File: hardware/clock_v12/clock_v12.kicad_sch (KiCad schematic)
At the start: 225 parts, among them J1 RJ45, J12 Conn_01x08_Pin, J14 Conn_01x02_Pin, J2 Conn_01x03, J4 USB_C_Receptacle, J5 Conn_01x06_Pin, J6 Conn_01x03_Pin, J8 Conn_01x02_Pin, Q1 2N7002, Q10 2N7002, Q9 2N7002, SW1 SW_Push_4PDT, SW2 SW_SPDT, U1 ADA4807-1, U10 STM32F405RGTx, U11 AMS1117-3.3, U12 BA50DD0WHFP-TR, U13 M24C02-RMN, U14 CH340C, U15 USBLC6-2P6, U16 TLV3603DCKR, U17 SN74LVC1G14DBV, U18 TMP112AIDRLR, U19 SN74LVC1G14DBV, U2 SN74LVC1G14DBV, U20 SN74LVC1G14DBV, U21 SN74LVC1G14DBV, U23 TPS63060, U3 SN74LVC1G14DBV, U4 ADA4807-1, U5 ADA4807-1, U6 TLV3603DCKR, U7 SN74LVC1G14DBV, U8 TLV3603DCKR, U9 L78L05_SOT89, Y1 MultiOsc, Y2 16MHz

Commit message: add 3d model for RJ45 connector
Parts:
- J1: footprint Connector_RJ:RJ45_Amphenol_RJHSE5380 -> blinky_footprints:RJ45_Amphenol_RJHSE5380
- J4: footprint Connector_USB:USB_C_Receptacle_HRO_TYPE-C-31-M-12 -> blinky_footprints:USB_C_Receptacle_HRO_TYPE-C-31-M-12
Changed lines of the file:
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@@
 			)
 		)
-		(property "Footprint" "Connector_USB:USB_C_Receptacle_HRO_TYPE-C-31-M-12"
+		(property "Footprint" "blinky_footprints:USB_C_Receptacle_HRO_TYPE-C-31-M-12"
 			(at 135.89 190.5 0)
 			(effects
@@
 			)
 		)
-		(property "Footprint" "Connector_RJ:RJ45_Amphenol_RJHSE5380"
+		(property "Footprint" "blinky_footprints:RJ45_Amphenol_RJHSE5380"
 			(at 30.48 247.015 90)
 			(effects

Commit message: update clock_v12 to kicad 8
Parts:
- D4: footprint Diode_SMD:D_SOD-523 -> Diode_SMD:D_SOD-123
- J4: footprint blinky_footprints:USB_C_Receptacle_HRO_TYPE-C-31-M-12 -> Connector_USB:USB_C_Receptacle_HRO_TYPE-C-31-M-12; JLCPCB Position Offset 0,1.3 -> 0,1.1
- U23: footprint blinky_footprints:Texas_S-PWSON-N10_ThermalVias-CJ -> Package_SON:Texas_S-PWSON-N10_ThermalVias
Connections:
- no-connect marks 39 -> 40
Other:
- moved on the sheet: C4, C46, C53, D4, J?, R4, R56, R57, TP1, TP10

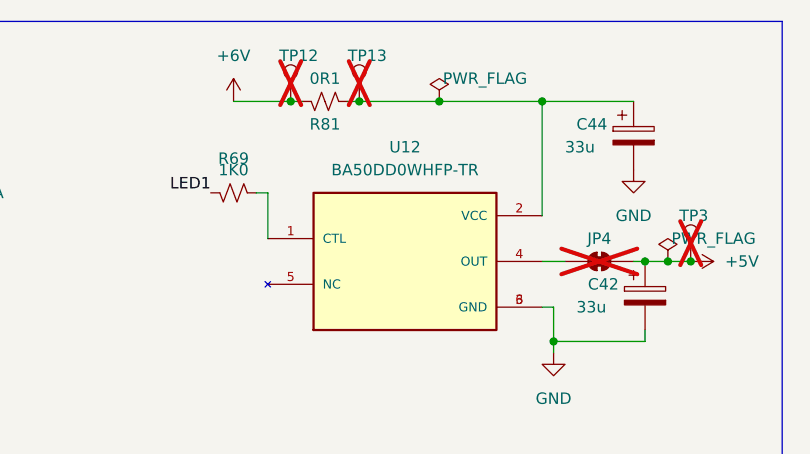
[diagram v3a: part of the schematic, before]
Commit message: clean up 3d models for clock
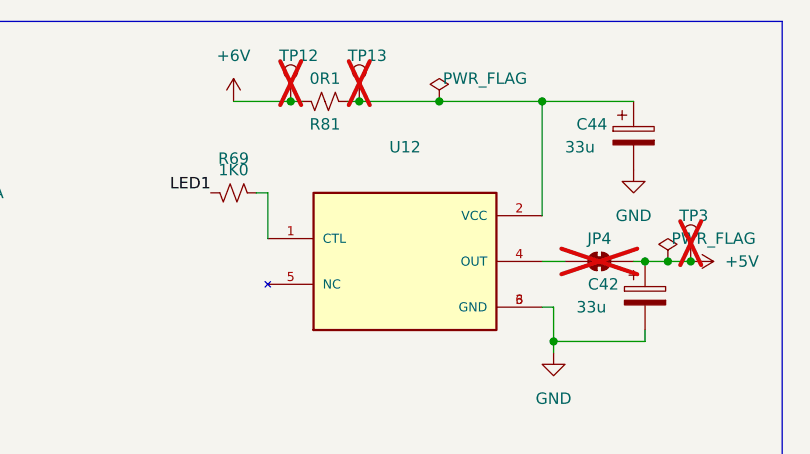
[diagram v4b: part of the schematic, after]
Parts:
- J4: footprint Connector_USB:USB_C_Receptacle_HRO_TYPE-C-31-M-12 -> blinky_footprints:USB_C_Receptacle_HRO_TYPE-C-31-M-12
- U12: footprint DPAK172P1054X200-6N -> blinky_footprints:DPAK172P1054X200-6N
- U16: footprint SC70_DCK_TEX -> blinky_footprints:SC70_DCK_TEX
- U23: footprint Package_SON:Texas_S-PWSON-N10_ThermalVias -> blinky_footprints:Texas_S-PWSON-N10_ThermalVias-CJ
- U6, U8: footprint SC70_DCK_TEX -> Package_TO_SOT_SMD:SOT-363_SC-70-6
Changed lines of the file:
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@@
 					(size 1.27 1.27)
 				)
+				(hide yes)
 			)
 		)
-		(property "Footprint" "DPAK172P1054X200-6N"
+		(property "Footprint" "blinky_footprints:DPAK172P1054X200-6N"
 			(at 125.73 44.45 0)
 			(effects
@@
 			)
 		)
-		(property "Footprint" "SC70_DCK_TEX"
+		(property "Footprint" "Package_TO_SOT_SMD:SOT-363_SC-70-6"
 			(at 99.06 245.11 0)
 			(effects
@@
 			)
 		)
-		(property "LCSC" ""
-			(at 99.06 245.11 0)
-			(effects
-				(font
-					(size 1.27 1.27)
-				)
-				(hide yes)
-			)
-		)
 		(property "JLCPCB Part #" "C5213955"
 			(at 99.06 245.11 0)
@@
 			)
 		)
-		(property "Footprint" "Package_SON:Texas_S-PWSON-N10_ThermalVias"
+		(property "Footprint" "blinky_footprints:Texas_S-PWSON-N10_ThermalVias-CJ"
 			(at 90.17 137.16 0)
 			(effects
@@
 			)
 		)
-		(property "Footprint" "Connector_USB:USB_C_Receptacle_HRO_TYPE-C-31-M-12"
+		(property "Footprint" "blinky_footprints:USB_C_Receptacle_HRO_TYPE-C-31-M-12"
 			(at 135.89 190.5 0)
 			(effects
@@
 			)
 		)
-		(property "Footprint" "SC70_DCK_TEX"
+		(property "Footprint" "Package_TO_SOT_SMD:SOT-363_SC-70-6"
 			(at 392.43 86.36 0)
 			(effects
@@
 			)
 		)
-		(property "Footprint" "SC70_DCK_TEX"
+		(property "Footprint" "blinky_footprints:SC70_DCK_TEX"
 			(at 421.64 38.1 0)
 			(effects
